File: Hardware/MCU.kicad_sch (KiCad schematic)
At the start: 16 parts, among them SW7 SW_Push, SW8 SW_Push, U16 ESP32-S3-WROOM-1

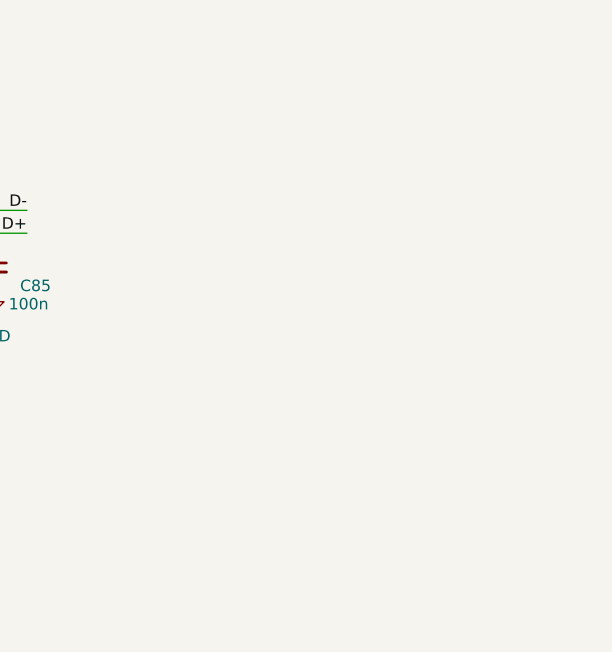
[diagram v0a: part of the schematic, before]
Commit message: cleaned up schematic hierarchy
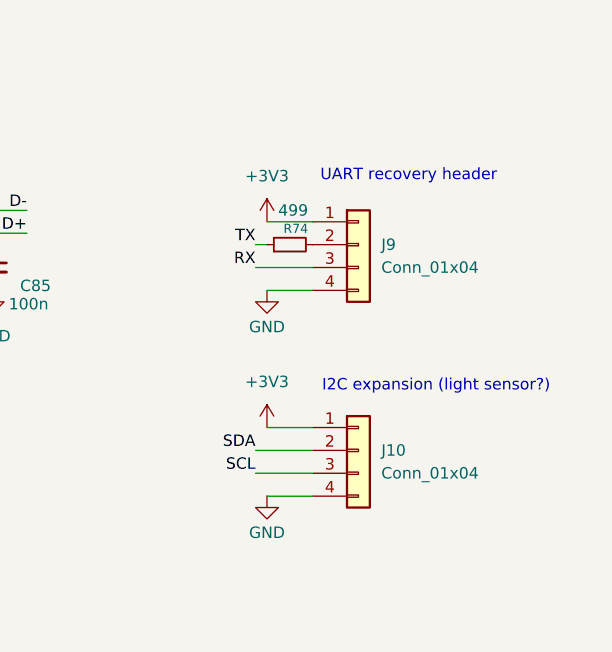
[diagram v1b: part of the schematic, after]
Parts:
- added J10, J9: Conn_01x04, symbol Connector_Generic:Conn_01x04
- added R74: 499, symbol Device:R_Small
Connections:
- net +3V3: now also J10.1 (Pin_1), J9.1 (Pin_1)
- net GND: now also J10.4 (Pin_4), J9.4 (Pin_4)
- net RX: now also J9.3 (Pin_3)
- net SCL: now also J10.3 (Pin_3)
- net SDA: now also J10.2 (Pin_2)
- net TX: now also R74.1
- new net: J9.2 (Pin_2), R74.2
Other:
- note added: "I2C expansion (light sensor?)"
- note added: "UART recovery header"

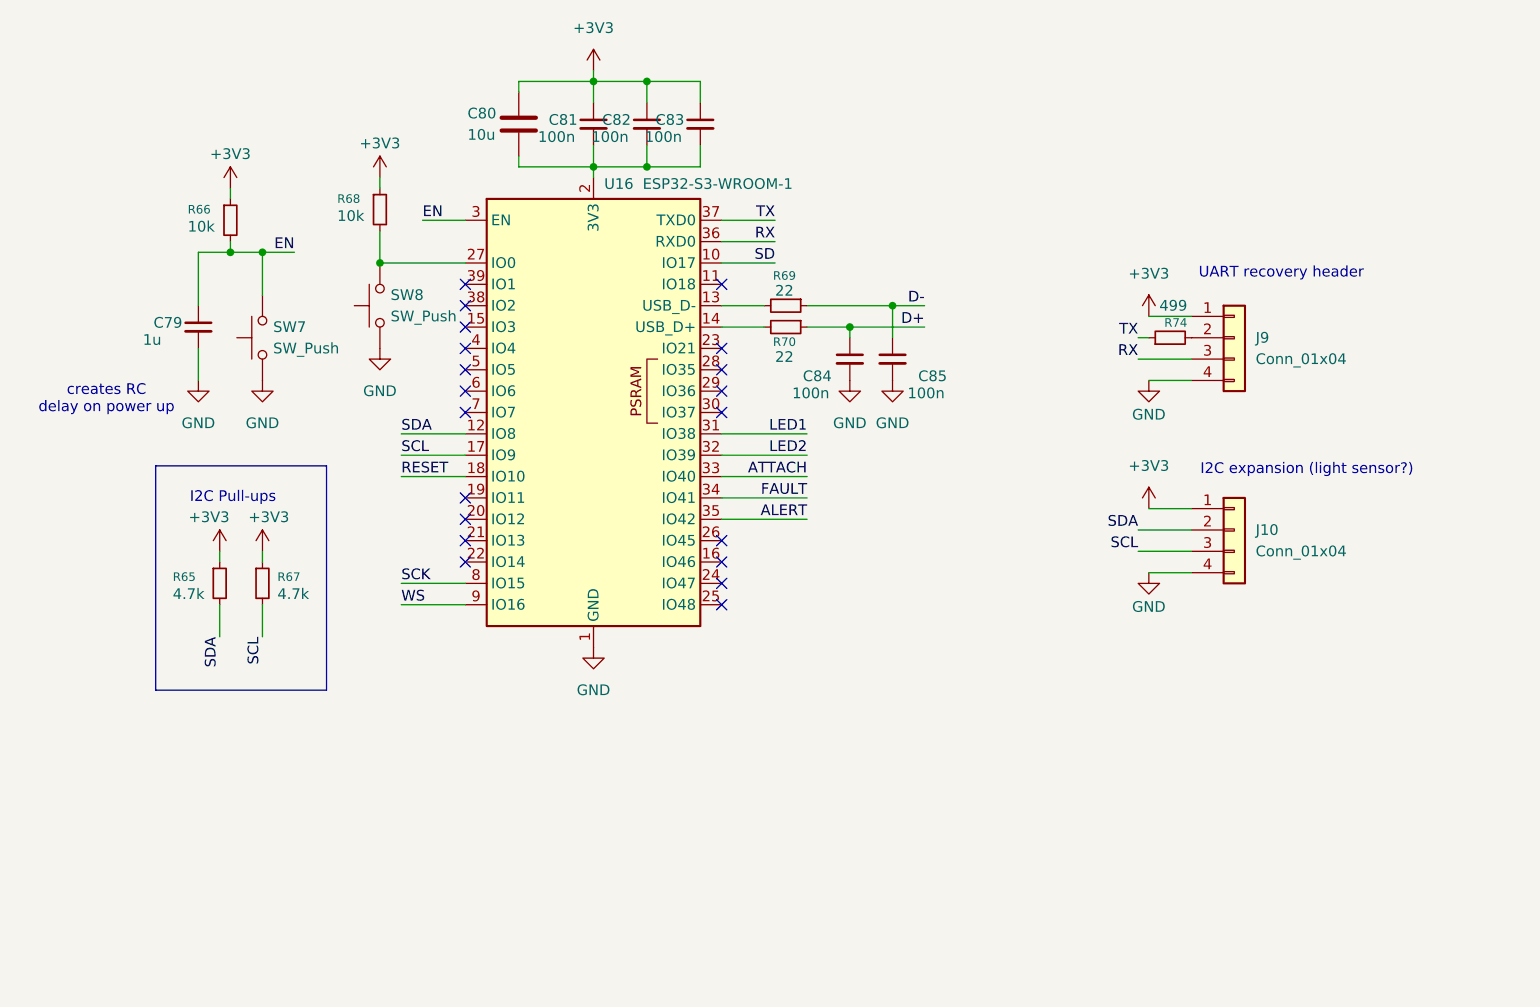
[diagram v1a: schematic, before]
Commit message: new buck ic with 6A current limit, more organization and changes
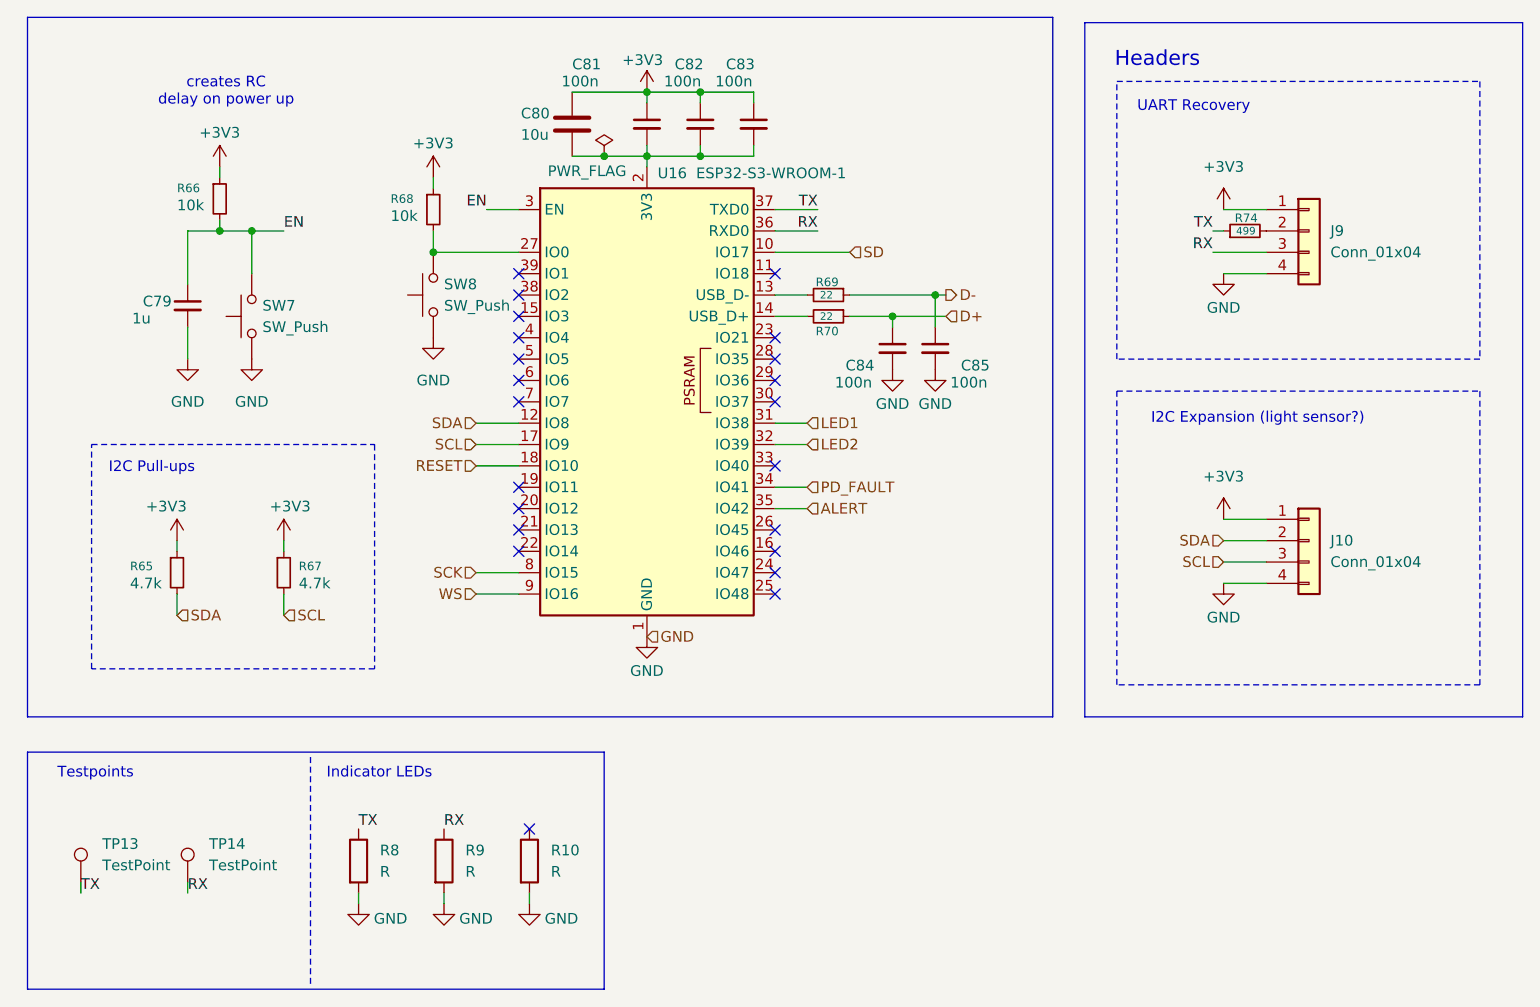
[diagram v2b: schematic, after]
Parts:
- added R10, R8, R9: R, symbol Device:R
- added TP13, TP14: TestPoint, symbol Connector:TestPoint
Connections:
- net GND: now also R10.2, R8.2, R9.2
- net RX: now also R9.1, TP14.1
- net TX: now also R8.1, TP13.1
- net ATTACH: no longer names the net of U16.33 (IO40)
- net FAULT renamed PD_FAULT
- no-connect marks 20 -> 22
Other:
- note added: "Headers"
- note added: "I2C Expansion (light sensor?)"
- note added: "Indicator LEDs"
- note added: "Testpoints"
- note added: "UART Recovery"
- note removed: "I2C expansion (light sensor?)"
- note removed: "UART recovery header"
- moved on the sheet: C79, C80, C81, C82, C83, C84, C85, J10, J9, R65, R66, R67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

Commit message: added more testpoints and indicator LEDs, added application notes
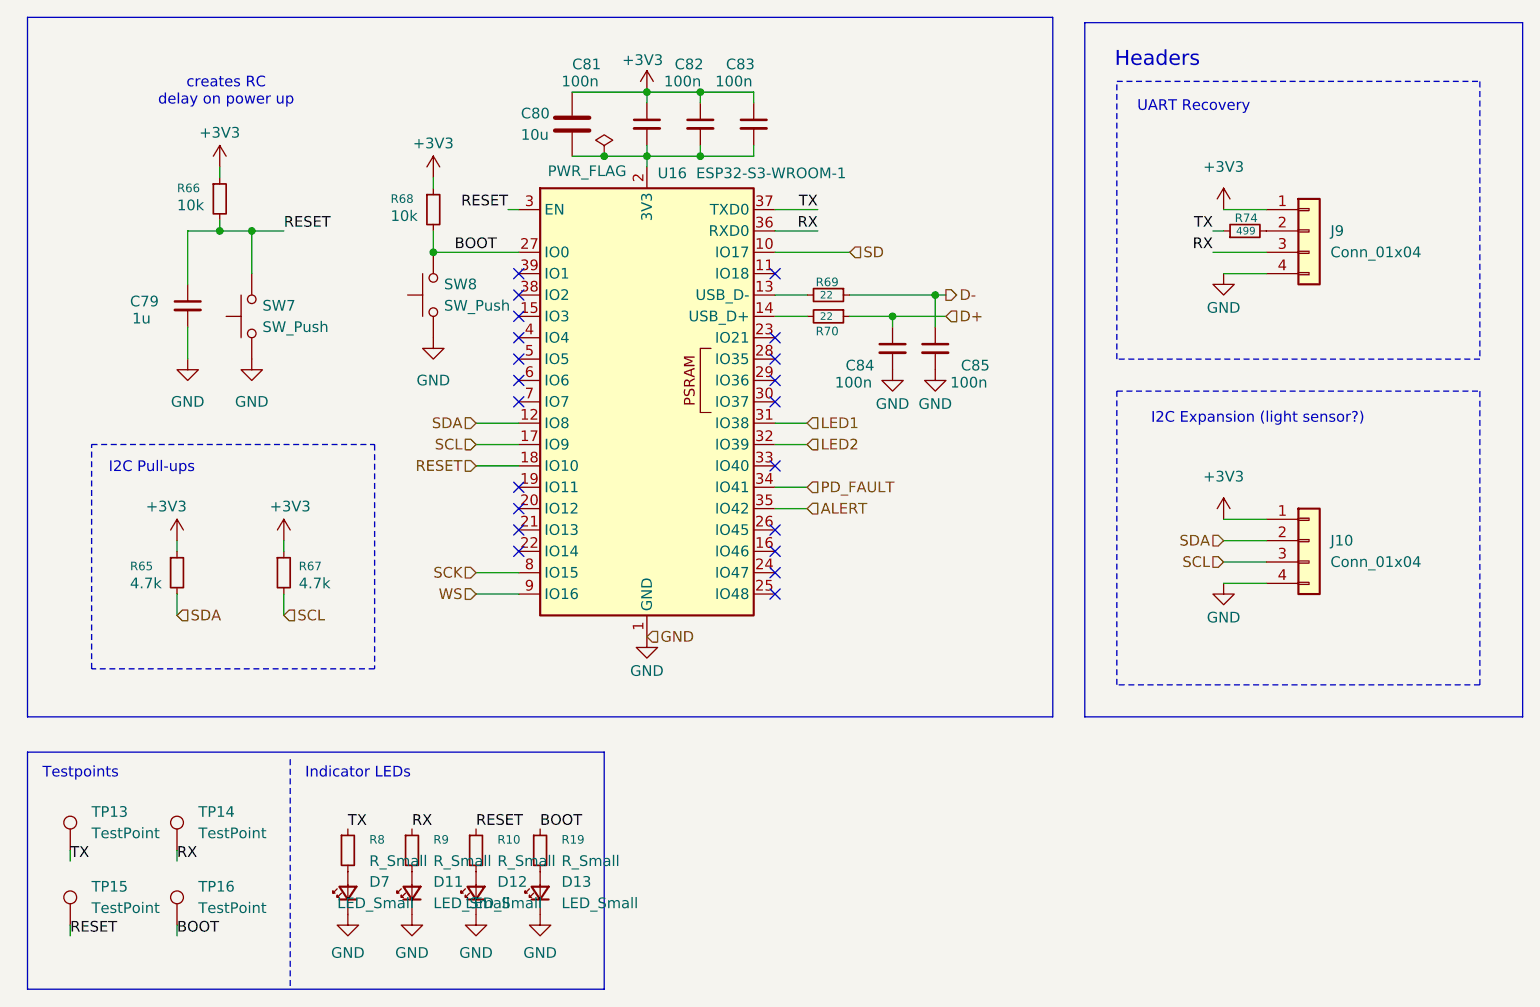
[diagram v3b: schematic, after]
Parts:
- removed R10, R8, R9: R, symbol Device:R
- added D11, D12, D13, D7: LED_Small, symbol Device:LED_Small
- added R10, R19, R8, R9: R_Small, symbol Device:R_Small
- added TP15, TP16: TestPoint, symbol Connector:TestPoint
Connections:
- net EN is gone; now on net RESET: C79.1, R66.2, SW7.2, U16.3 (EN)
- net GND: now also D11.1 (K), D12.1 (K), D13.1 (K), D7.1 (K)
- net RESET: now also R10.1, TP15.1
- net RX: now also R9.1
- net TX: now also R8.1
- net BOOT: now reaches R68.2, SW8.2, U16.27 (IO0)
- net BOOT: now also R19.1, TP16.1
- new net: D13.2 (A), R19.2
- new net: D11.2 (A), R9.2
- new net: D7.2 (A), R8.2
- new net: D12.2 (A), R10.2
- no-connect marks 22 -> 21
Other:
- moved on the sheet: TP13, TP14
